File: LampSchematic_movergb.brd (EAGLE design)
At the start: 51.6 x 45 mm, 29 parts, among them U1 ATTINY84-20SSU, U2 VEML6040, U3 PMV20ENR, U5 Si3417DV, X2 1751248

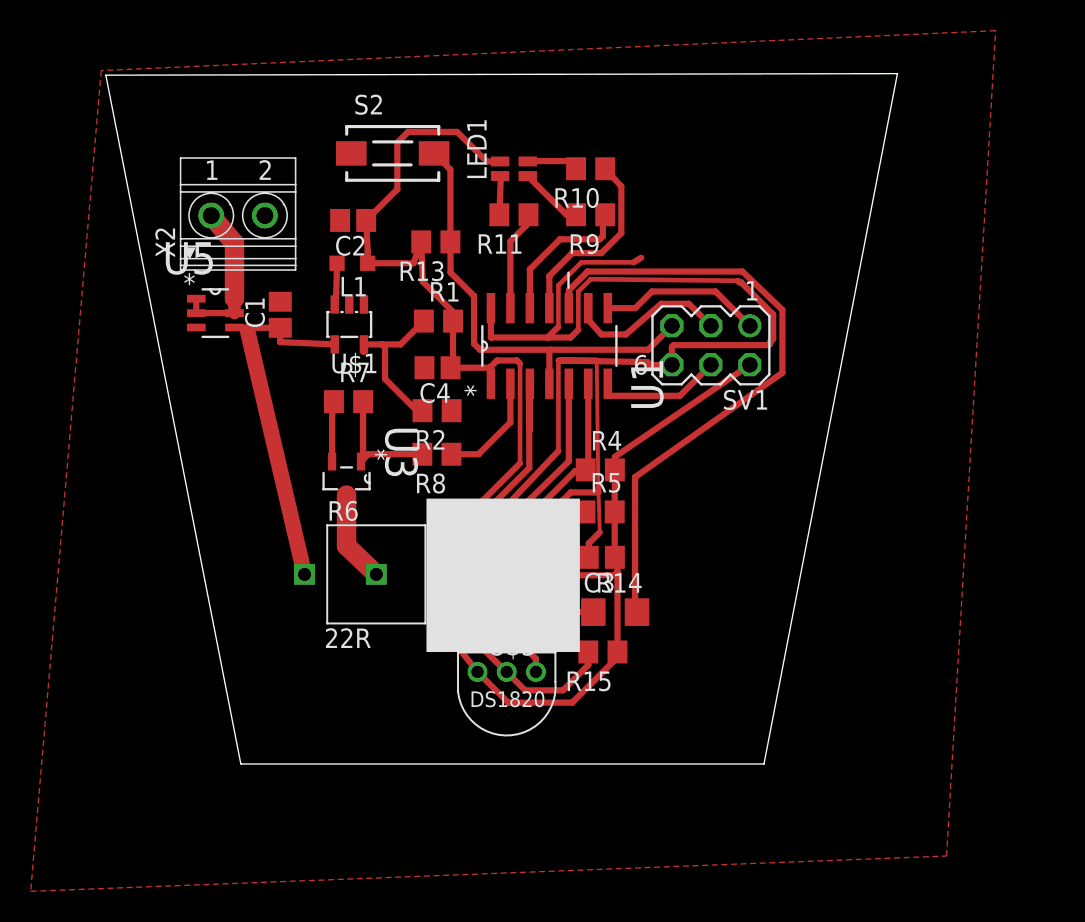
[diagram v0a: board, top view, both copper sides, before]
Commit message: updates the LAMP stuff
Better layout for the PCB
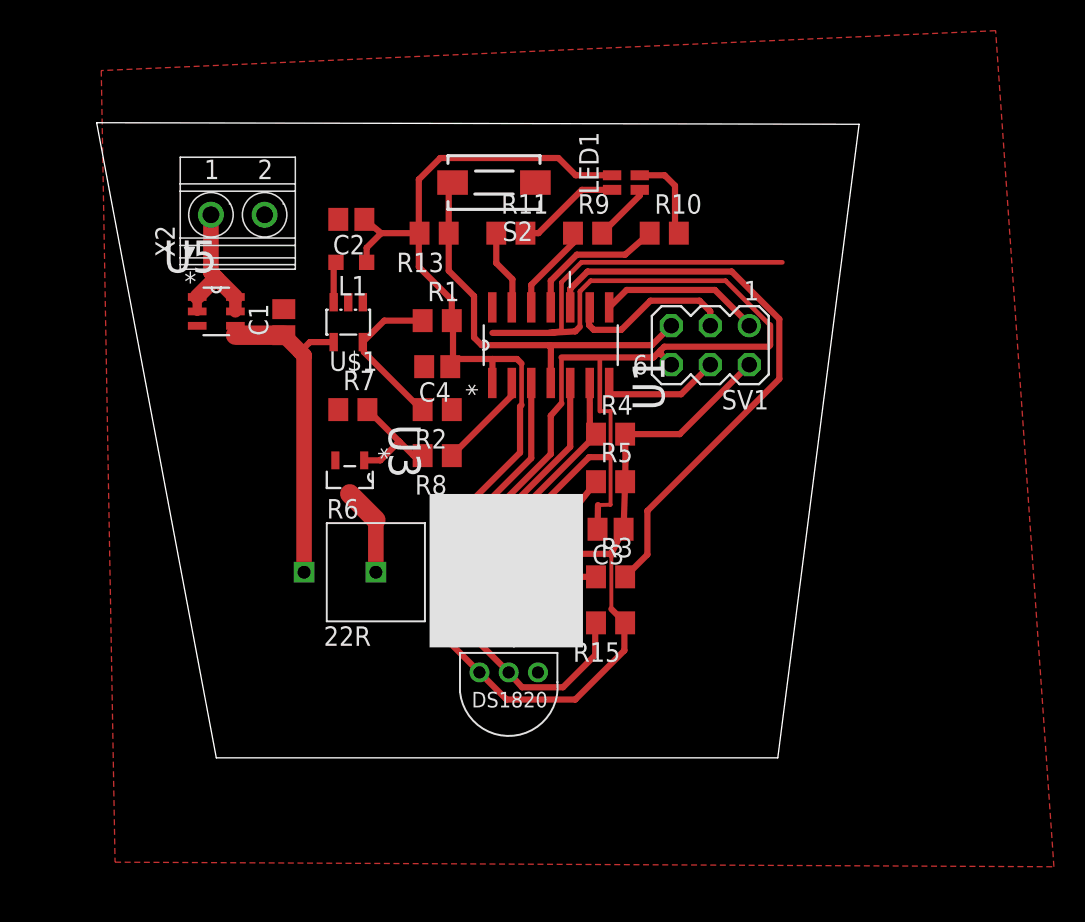
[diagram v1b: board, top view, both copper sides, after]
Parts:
- removed R14: 4.7k, resistor:R1206
- added R3: 6.8R, resistor:R0805
- C1: value (none) -> 0.1uF
- SV1: value (none) -> ISP
- moved LED1 7.36 mm to (57.3, 51.6)
- moved S2 6.87 mm to (48.7, 51.6), turned to 180 degrees
- moved R10 6.38 mm to (59.8, 48.3), turned to 0 degrees
- moved R4 2.42 mm to (56.3, 35.2)
- moved R5 2.08 mm to (56.3, 32.1)
- moved R15 1.96 mm to (56.3, 22.9)
- moved C3 1.92 mm to (56.3, 29.0)
- moved R11 1.22 mm to (49.8, 48.3), turned to 0 degrees
- moved R9 1.22 mm to (54.8, 48.3), turned to 0 degrees
- moved U$3 0.75 mm to (49.6, 24.7)
- moved R7 0.59 mm to (39.5, 36.8)
- moved R13 0.58 mm to (44.8, 48.3)
- moved C1 0.53 mm to (35.0, 42.5)
- moved U3 0.22 mm to (39.3, 32.4)
- moved U$1 0.17 mm to (39.2, 42.5)
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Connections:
- net N$9: now also R3.1; no longer R14.1
- net UV: now also R3.2; no longer R14.2
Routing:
- net GND: track 102.1 -> 92.9 mm
- net UV: track 41.9 -> 37.6 mm
- net N$8: track 2.55 -> 6.82 mm
- net VCC: track 103.8 -> 107.5 mm
- net RED: track 9.69 -> 6.00 mm
- net GREEN: track 12.5 -> 9.42 mm
- net RES: track 29.4 -> 27.0 mm
- net N$7: track 3.59 -> 5.88 mm
- net +12V: track 24.1 -> 22.2 mm
- net SCLK: track 20.6 -> 22.2 mm
- net N$9: track 4.27 -> 5.74 mm
- net BLUE: track 6.62 -> 5.29 mm
- net TEMP: track 32.3 -> 31.2 mm
- net HEAT: track 7.22 -> 6.36 mm
- net SCK: track 10.5 -> 11.2 mm
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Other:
- board size 51.6 x 45 mm -> 49.7 x 41.4 mm
